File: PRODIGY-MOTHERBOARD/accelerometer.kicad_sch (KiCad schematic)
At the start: 1 part, among them U11 LIS2DH

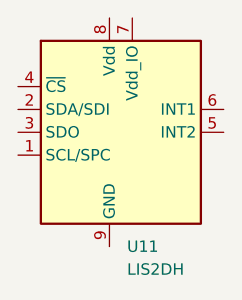
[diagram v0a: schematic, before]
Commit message: project restructure done. Hierarchical sheet done. Outputs/breakouts sheet done
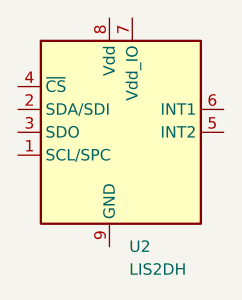
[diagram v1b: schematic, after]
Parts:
- renumbered U11 to U2
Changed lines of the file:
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@@
-(kicad_sch (version 20230121) (generator eeschema)
-  (paper "A4")
-  (symbol (lib_id "Sensor_Motion:LIS2DH") (at 137.16 83.82 0) (unit 1)
-    (in_bom yes) (on_board yes) (dnp no) (fields_autoplaced)
-    (property "Reference" "U11" (at 139.1159 96.52 0)
-      (effects (font (size 1.27 1.27)) (justify left))
-    )
-    (property "Value" "LIS2DH" (at 139.1159 99.06 0)
-      (effects (font (size 1.27 1.27)) (justify left))
-    )
-    (property "Footprint" "Package_LGA:LGA-14_2x2mm_P0.35mm_LayoutBorder3x4y" (at 137.16 95.25 0)
-      (effects (font (size 1.27 1.27)) hide)
-    )
-    (property "Datasheet" "http://www.st.com/web/en/resource/technical/document/datasheet/DM00042751.pdf" (at 137.16 99.06 0)
-      (effects (font (size 1.27 1.27)) hide)
-    )
-    (pin "1")
-    (pin "10")
-    (pin "11")
-    (pin "12")
-    (pin "13")
-    (pin "14")
-    (pin "2")
-    (pin "3")
-    (pin "4")
-    (pin "5")
-    (pin "6")
-    (pin "7")
-    (pin "8")
-    (pin "9")
-    (instances
-      (project "PRODIGY-MOTHERBOARD"
-        (path "/f1c25860-8989-4190-bd24-2491d23ca7d9/47725dfe-8a89-438d-9e4f-9e943dfd0098"
-          (reference "U11") (unit 1)
-        )
-      )
-    )
-  )
+(kicad_sch
+	(version 20231120)
+	(generator "eeschema")
+	(generator_version "8.0")
+	(paper "A4")
+	(symbol
+		(lib_id "Sensor_Motion:LIS2DH")
+		(at 137.16 83.82 0)
+		(unit 1)
+		(exclude_from_sim no)
+		(in_bom yes)
+		(on_board yes)
+		(dnp no)
+		(fields_autoplaced yes)
+		(property "Reference" "U2"
+			(at 139.3541 96.52 0)
+			(effects
+				(font
+					(size 1.27 1.27)
+				)
+				(justify left)
+			)
+		)
+		(property "Value" "LIS2DH"
+			(at 139.3541 99.06 0)
+			(effects
+				(font
+					(size 1.27 1.27)
+				)
+				(justify left)
+			)
+		)
+		(property "Footprint" "Package_LGA:LGA-14_2x2mm_P0.35mm_LayoutBorder3x4y"
+			(at 137.16 95.25 0)
+			(effects
+				(font
+					(size 1.27 1.27)
+				)
+				(hide yes)
+			)
+		)
+		(property "Datasheet" "http://www.st.com/web/en/resource/technical/document/datasheet/DM00042751.pdf"
+			(at 137.16 99.06 0)
+			(effects
+				(font
+					(size 1.27 1.27)
+				)
+				(hide yes)
+			)
+		)
+		(property "Description" ""
+			(at 137.16 83.82 0)
+			(effects
+				(font
+					(size 1.27 1.27)
+				)
+				(hide yes)
+			)
+		)
+		(pin "1"
+		)
+		(pin "10"
+		)
+		(pin "11"
+		)
+		(pin "12"
+		)
+		(pin "13"
+		)
+		(pin "14"
+		)
+		(pin "2"
+		)
+		(pin "3"
+		)
+		(pin "4"
+		)
+		(pin "5"
+		)
+		(pin "6"
+		)
+		(pin "7"
+		)
+		(pin "8"
+		)
+		(pin "9"
+		)
+		(instances
+			(project "PRODIGY-MOTHERBOARD"
+				(path "/f1c25860-8989-4190-bd24-2491d23ca7d9/e2913798-f444-47a6-8b64-53020d7d816b/c2afee45-57e5-4466-9ef1-0a43aa29e9a3"
+					(reference "U2")
+					(unit 1)
+				)
+			)
+		)
+	)
 )
